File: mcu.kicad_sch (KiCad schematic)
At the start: 35 parts, among them J10 Conn_01x01_Pin, J11 Conn_01x01_Pin, J12 Conn_01x01_Pin, J13 Conn_01x01_Pin, J14 Conn_01x01_Pin, J15 Conn_01x01_Pin, J16 Conn_01x01_Pin, J3 Conn_01x02_Pin, J5 Conn_01x04_Pin, J7 Conn_01x01_Pin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

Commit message: T.
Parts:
- U17: footprint PSG:20x4 screen -> PSG:2x16_vertical
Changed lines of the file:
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@@
 			)
 		)
-		(property "Footprint" "PSG:20x4 screen"
+		(property "Footprint" "PSG:2x16_vertical"
 			(at 264.668 125.984 0)
 			(effects

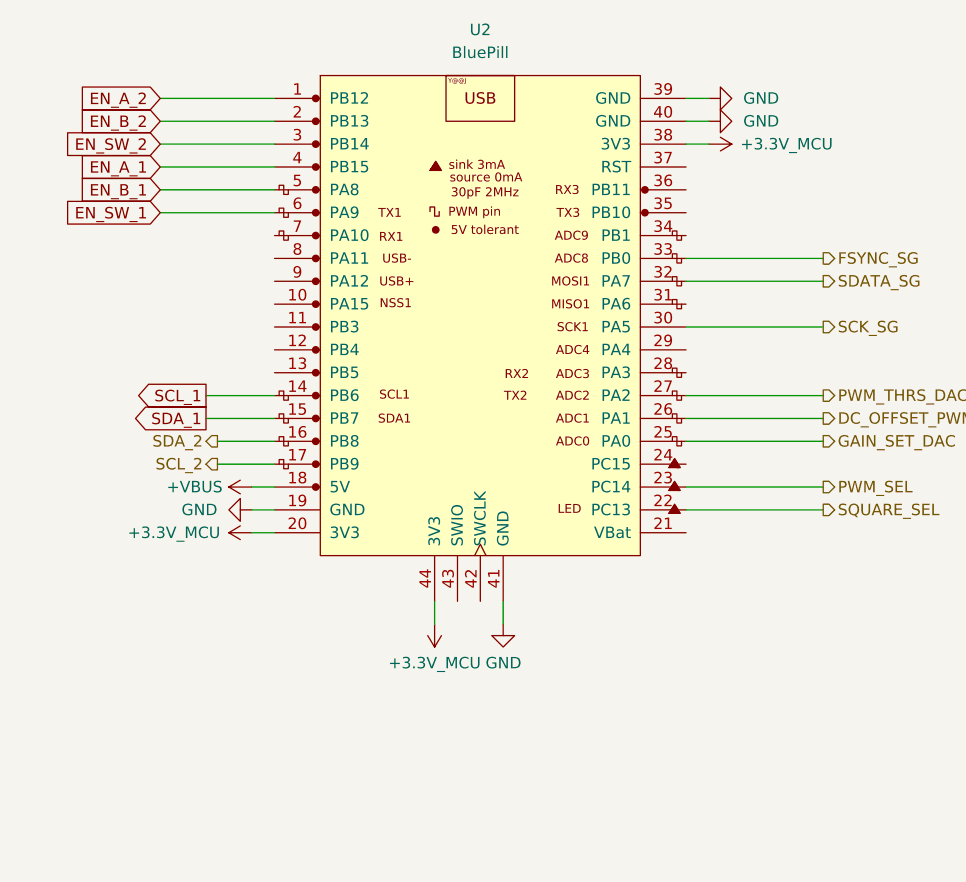
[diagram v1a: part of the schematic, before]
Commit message: Add the tested push-pull rail generator.
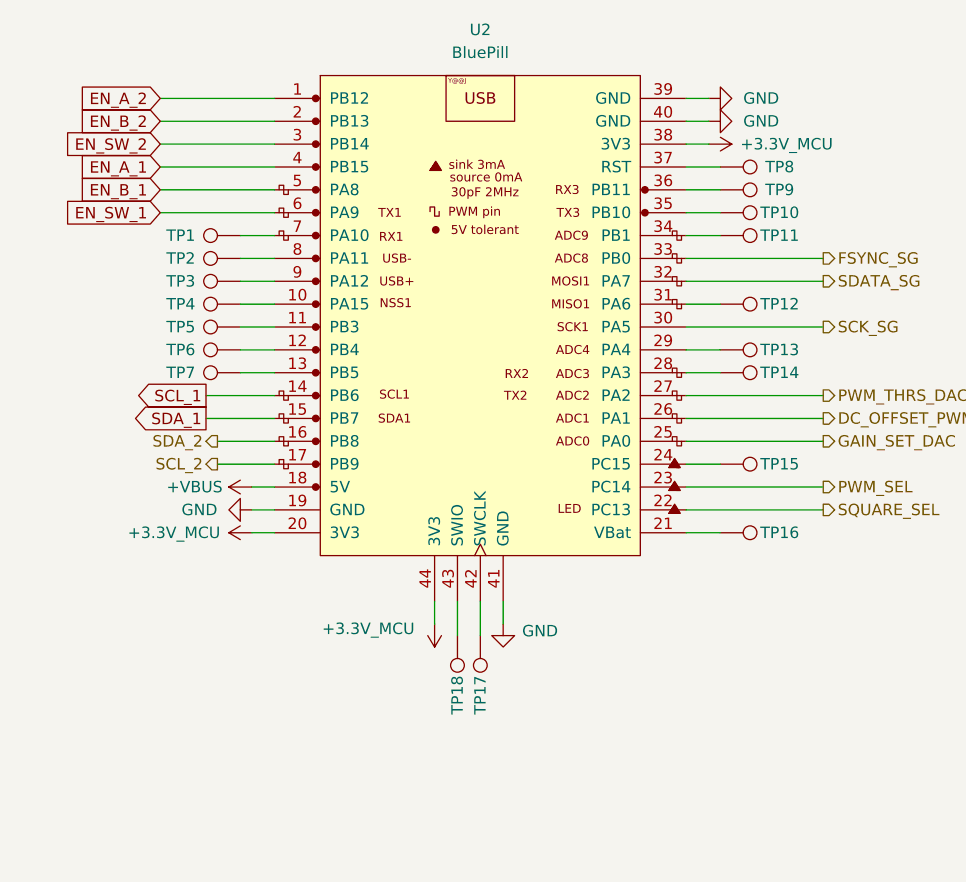
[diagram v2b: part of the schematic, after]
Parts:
- added TP1, TP10, TP11, TP12, TP13, TP14, TP15, TP16, TP17, TP18, TP2, TP3, TP4, TP5, TP6, TP7, TP8, TP9: TestPoint, TestPoint:TestPoint_Pad_D3.0mm, symbol Connector:TestPoint
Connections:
- net at U2.10 (PA15): now also TP4.1
- net at U2.11 (PB3): now also TP5.1
- net at U2.12 (PB4): now also TP6.1
- net at U2.13 (PB5): now also TP7.1
- net at U2.21 (VBat): now also TP16.1
- net at U2.24 (PC15): now also TP15.1
- net at U2.28 (PA3): now also TP14.1
- net at U2.29 (PA4): now also TP13.1
- net at U2.31 (PA6): now also TP12.1
- net at U2.34 (PB1): now also TP11.1
- net at U2.35 (PB10): now also TP10.1
- net at U2.36 (PB11): now also TP9.1
- net at U2.37 (RST): now also TP8.1
- net at U2.42 (SWCLK): now also TP17.1
- net at U2.43 (SWIO): now also TP18.1
- net at U2.7 (PA10): now also TP1.1
- net at U2.8 (PA11): now also TP2.1
- net at U2.9 (PA12): now also TP3.1
